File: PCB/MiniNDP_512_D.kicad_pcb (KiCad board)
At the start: 2 copper layers, 60 x 34 mm, 21 parts, among them J1 Conn_02x20_Odd_Even, U1 HC138, U2 4040, U3 FCT821, U4 AS6C4008, U5 2G04, U6 1G32

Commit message: D board routing
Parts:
- moved R1 0.19 mm to (147.9, 106.5)
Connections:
- U5 pad 1: /~{BYTE} -> /~{BLOCK}
- U5 pad 3: /~{BLOCK} -> /~{BYTE}
- U5 pad 4: /BLOCK -> /BYTE
- U5 pad 6: /BYTE -> /BLOCK
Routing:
- net /~{BLOCK}: track 57.7 -> 54.3 mm
- net /BYTE: track 14.4 -> 12.4 mm
- net /BLOCK: track 11.1 -> 12.9 mm
- net /~{BYTE}: track 36.8 -> 38.4 mm
- net GND: vias 34 -> 32

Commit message: E board
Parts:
- moved C4 0.06 mm to (123.8, 100.2)
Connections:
- net /BLOCK renamed /BYTE0
- net /BYTE renamed /~{BYTE++}
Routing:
- net GND: vias 32 -> 31

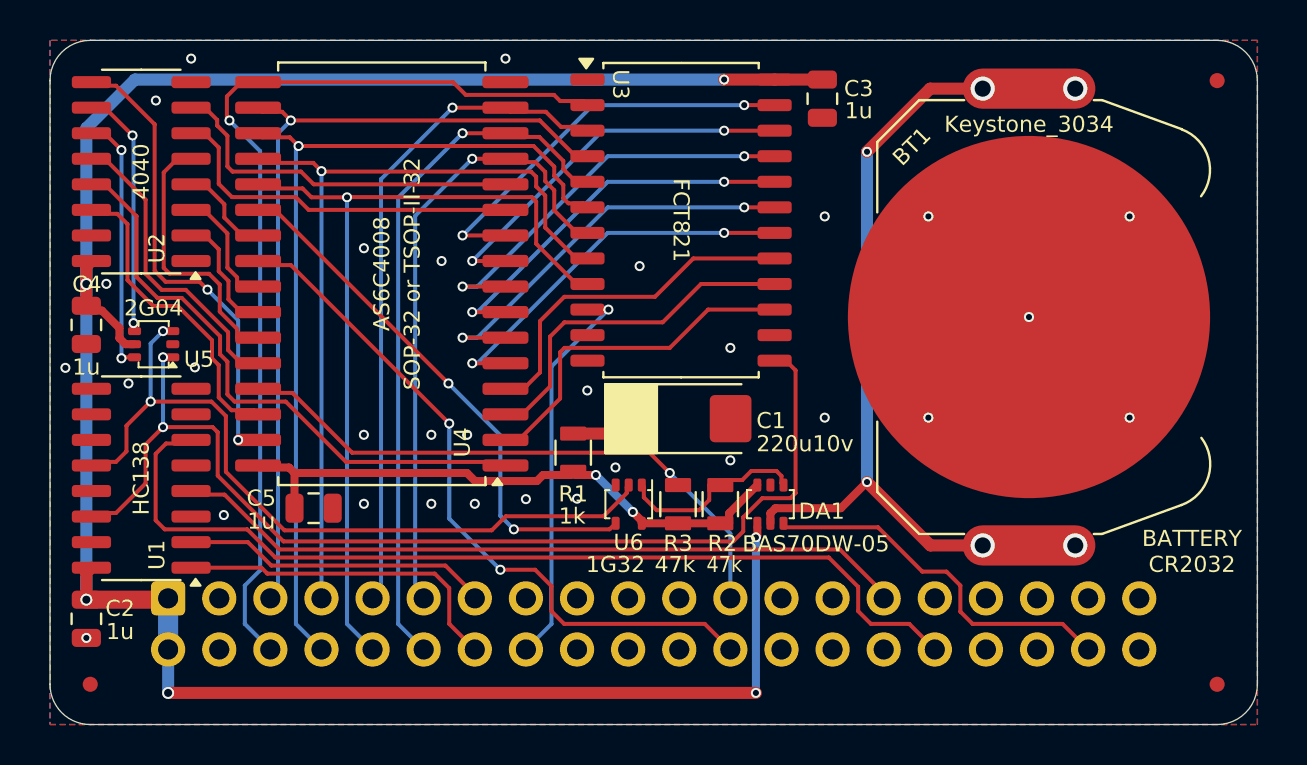
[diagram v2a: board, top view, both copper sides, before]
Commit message: make E version default, easier to solder
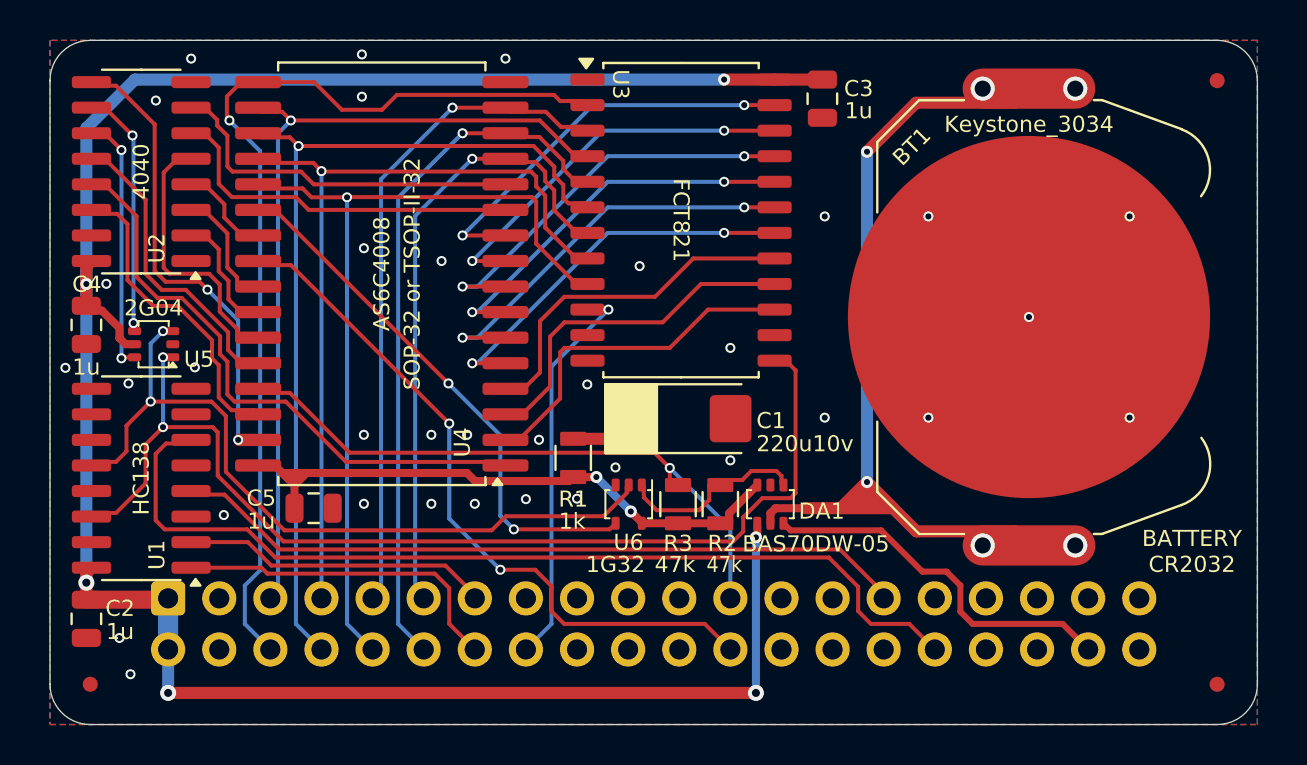
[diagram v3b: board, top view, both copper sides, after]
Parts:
- removed ENCLOSURE: MiniNDP_Cover, 000_LOCAL:MiniNDP_Cover
- added N1: MiniNDP_Cover, 000_LOCAL:MiniNDP_Cover, F.Cu at (151.9, 103.0)
- moved R1 0.26 mm to (147.9, 106.8)
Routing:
- net VBUS: track 114.8 -> 113.9 mm
- net /AD0: track 47.7 -> 48.3 mm
- net GND: vias 31 -> 35
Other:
- board text removed: "cover"

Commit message: larger parts on D version and proper bom
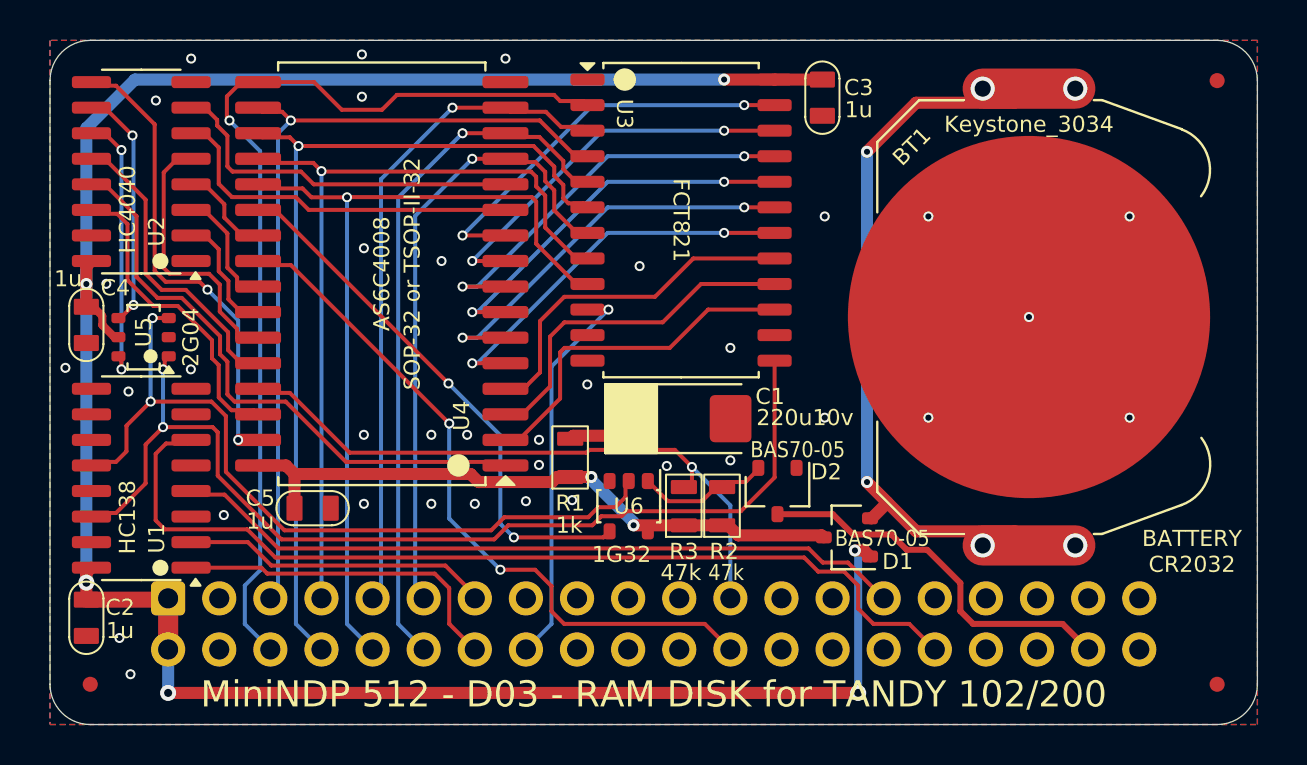
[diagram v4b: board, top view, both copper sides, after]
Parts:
- removed DA1: BAS70DW-05, 000_LOCAL:SOT-363_SC-70-6_symmetric
- added D1: BAS70-05, 000_LOCAL:SOT-23, F.Cu at (161.6, 110.7)
- added D2: BAS70-05, 000_LOCAL:SOT-23, F.Cu at (158.1, 108.4)
- U2: value 4040 -> HC4040
- U5: footprint 000_LOCAL:SOT-363_SC-70-6 -> 000_LOCAL:TSOP-6_1.65x3.05mm_P0.95mm
- U6: footprint 000_LOCAL:SOT-353_SC-70-5 -> 000_LOCAL:SOT-23-5
- moved U5 0.61 mm to (126.6, 100.8)
- moved R3 0.31 mm to (153.4, 109.2)
- moved R1 0.15 mm to (147.8, 106.8)
- moved R2 0.14 mm to (155.3, 109.2)
- moved U6 0.10 mm to (150.7, 109.2)
- moved C3 0.05 mm to (160.3, 88.9)
- moved C5 0.05 mm to (135.0, 109.3)
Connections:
- net /~{BYTE++} renamed /BYTE++
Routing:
- net VBUS: track 113.9 -> 117.8 mm
- net +BATT: track 41.1 -> 37.8 mm
- net /~{BLOCK}: track 54.3 -> 51.2 mm
- net /SLEEP: track 9.59 -> 6.63 mm
- net VMEM: track 29.0 -> 31.7 mm
- net /~{BYTE}: track 38.4 -> 39.4 mm
- net /~{WR}: track 31.1 -> 32.0 mm
- net /BYTE0: track 12.9 -> 13.4 mm
- net /RAMRST: track 18.5 -> 19.0 mm
- net GND: vias 35 -> 36
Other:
- board text added: "${TITLE} - ${REVISION} - RAM DISK for TANDY 102/200"
- board text added: "100 1 CLEAR0,61558:T=61558:E=62957:OUT129,2 200 1 CLEAR0,59715:T=59715:E=61101:OUT129,2 2 FORA=0TO15:N=INP(131):NEXT:FORA=TTOE 3 POKEA,INP(131):IFA=T+1007THENOUT129,1 4 ?{dblquote}.{dblquote};:NEXT:SAVEM{dblquote}RAMDSK{dblquote},T,E,T"
- board text added: "Bootstrap RAMDSK from BANK 0. For BANK 1 change OUT129 to OUT133. RAM100.CO or RAM200.CO must be the first file in the bank."
- board text added: "RAM DISK for TANDY 102/200"
